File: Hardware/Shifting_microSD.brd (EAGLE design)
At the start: 18.3 x 25.1 mm, 20 parts, among them J1 USD_CONNECTOR, U1 TXB0104, U2 3.3V

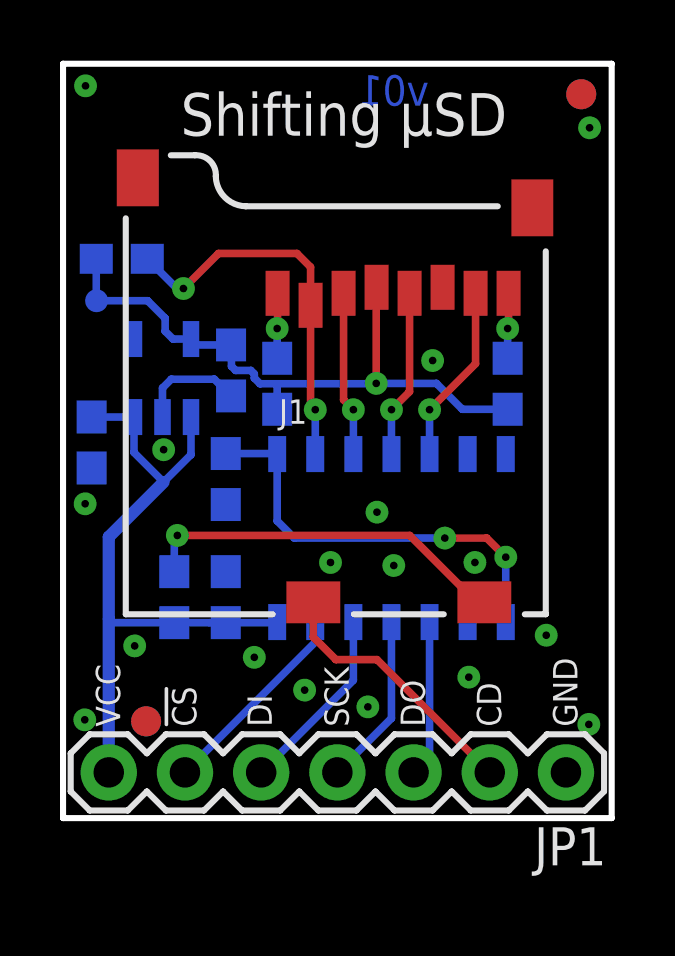
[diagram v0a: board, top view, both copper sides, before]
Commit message: Connected both 3.3V nets
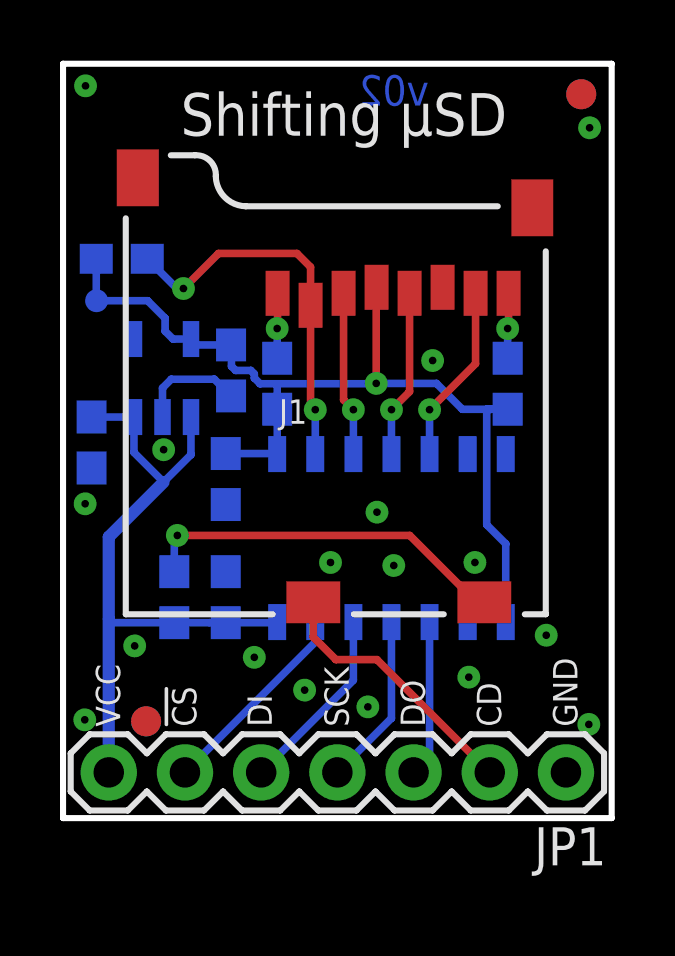
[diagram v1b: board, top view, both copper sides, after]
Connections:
- removed net 3.3V: C4.1, U1.1, U1.8
- net 3V3: now also C4.1, U1.1, U1.8
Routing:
- net 3.3V: track 14.2 -> 0.00 mm, vias 2 -> 0
- net 3V3: track 21.4 -> 32.7 mm
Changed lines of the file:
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@@
 <layers>
 <layer number="1" name="Top" color="4" fill="1" visible="yes" active="yes"/>
-<layer number="2" name="Route2" color="1" fill="3" visible="yes" active="yes"/>
-<layer number="3" name="Route3" color="4" fill="3" visible="yes" active="yes"/>
-<layer number="4" name="Route4" color="1" fill="4" visible="yes" active="yes"/>
-<layer number="5" name="Route5" color="4" fill="4" visible="yes" active="yes"/>
-<layer number="6" name="Route6" color="1" fill="8" visible="yes" active="yes"/>
-<layer number="7" name="Route7" color="4" fill="8" visible="yes" active="yes"/>
-<layer number="8" name="Route8" color="1" fill="2" visible="yes" active="yes"/>
-<layer number="9" name="Route9" color="4" fill="2" visible="yes" active="yes"/>
-<layer number="10" name="Route10" color="1" fill="7" visible="yes" active="yes"/>
-<layer number="11" name="Route11" color="4" fill="7" visible="yes" active="yes"/>
-<layer number="12" name="Route12" color="1" fill="5" visible="yes" active="yes"/>
-<layer number="13" name="Route13" color="4" fill="5" visible="yes" active="yes"/>
-<layer number="14" name="Route14" color="1" fill="6" visible="yes" active="yes"/>
-<layer number="15" name="Route15" color="4" fill="6" visible="yes" active="yes"/>
 <layer number="16" name="Bottom" color="1" fill="1" visible="yes" active="yes"/>
 <layer number="17" name="Pads" color="2" fill="1" visible="yes" active="yes"/>
@@
 </plain>
 <attributes>
-<attribute name="VERSION" value="v01"/>
+<attribute name="VERSION" value="v02"/>
 </attributes>
 <variantdefs>
@@
 <wire x1="1.1312" y1="17.2466" x2="1.1058" y2="17.272" width="0.254" layer="16"/>
 <wire x1="1.1312" y1="17.2466" x2="1.1176" y2="17.2466" width="0.254" layer="16"/>
+<contactref element="U1" pad="8"/>
+<contactref element="U1" pad="1"/>
+<wire x1="7.1374" y1="13.628" x2="7.1374" y2="12.1345" width="0.254" layer="16"/>
+<wire x1="14.8209" y1="13.628" x2="14.1224" y2="13.628" width="0.254" layer="16"/>
+<wire x1="14.1224" y1="13.628" x2="14.1224" y2="9.779" width="0.254" layer="16"/>
+<wire x1="14.1224" y1="9.779" x2="14.7574" y2="9.144" width="0.254" layer="16"/>
+<wire x1="14.7574" y1="9.144" x2="14.7574" y2="6.5345" width="0.254" layer="16"/>
+<contactref element="C4" pad="1"/>
+<wire x1="5.4229" y1="12.153" x2="7.1189" y2="12.153" width="0.254" layer="16"/>
+<wire x1="7.1189" y1="12.153" x2="7.1374" y2="12.1345" width="0.254" layer="16"/>
 </signal>
 <signal name="!CS_3V3">
@@
 <wire x1="3.7084" y1="6.516" x2="4.8768" y2="6.516" width="0.254" layer="16"/>
 </signal>
-<signal name="3.3V">
-<contactref element="U1" pad="1"/>
-<contactref element="C4" pad="1"/>
-<contactref element="U1" pad="8"/>
-<wire x1="5.4229" y1="12.153" x2="7.1189" y2="12.153" width="0.254" layer="16"/>
-<wire x1="7.1189" y1="12.153" x2="7.1374" y2="12.1345" width="0.254" layer="16"/>
-<wire x1="7.1374" y1="12.1345" x2="7.1374" y2="9.906" width="0.254" layer="16"/>
-<wire x1="7.1374" y1="9.906" x2="7.7089" y2="9.3345" width="0.254" layer="16"/>
-<wire x1="7.7089" y1="9.3345" x2="12.7254" y2="9.3345" width="0.254" layer="16"/>
-<wire x1="14.7574" y1="8.6995" x2="14.7574" y2="6.5345" width="0.254" layer="16"/>
-<via x="12.7254" y="9.3345" extent="1-16" drill="0.254"/>
-<wire x1="12.7254" y1="9.3345" x2="14.1224" y2="9.3345" width="0.254" layer="1"/>
-<wire x1="14.1224" y1="9.3345" x2="14.7574" y2="8.6995" width="0.254" layer="1"/>
-<via x="14.7574" y="8.6995" extent="1-16" drill="0.254"/>
-</signal>
 <signal name="SCK_3V3">

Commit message: Incremented to v10
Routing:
- net GND: vias 17 -> 18
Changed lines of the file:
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@@
 <setting verticaltext="up"/>
 </settings>
-<grid distance="0.001" unitdist="inch" unit="inch" style="lines" multiple="1" display="yes" altdistance="0.001" altunitdist="inch" altunit="inch"/>
+<grid distance="0.001" unitdist="inch" unit="mil" style="lines" multiple="1" display="yes" altdistance="0.001" altunitdist="inch" altunit="inch"/>
 <layers>
 <layer number="1" name="Top" color="4" fill="1" visible="yes" active="yes"/>
@@
 </plain>
 <attributes>
-<attribute name="VERSION" value="v02"/>
+<attribute name="VERSION" value="v10"/>
 </attributes>
 <variantdefs>
@@
 <via x="3.3528" y="12.2809" extent="1-16" drill="0.254"/>
 <via x="12.319" y="15.2527" extent="1-16" drill="0.254"/>
+<via x="14.9098" y="10.1473" extent="1-16" drill="0.254"/>
 </signal>
 <signal name="VDD_IO">

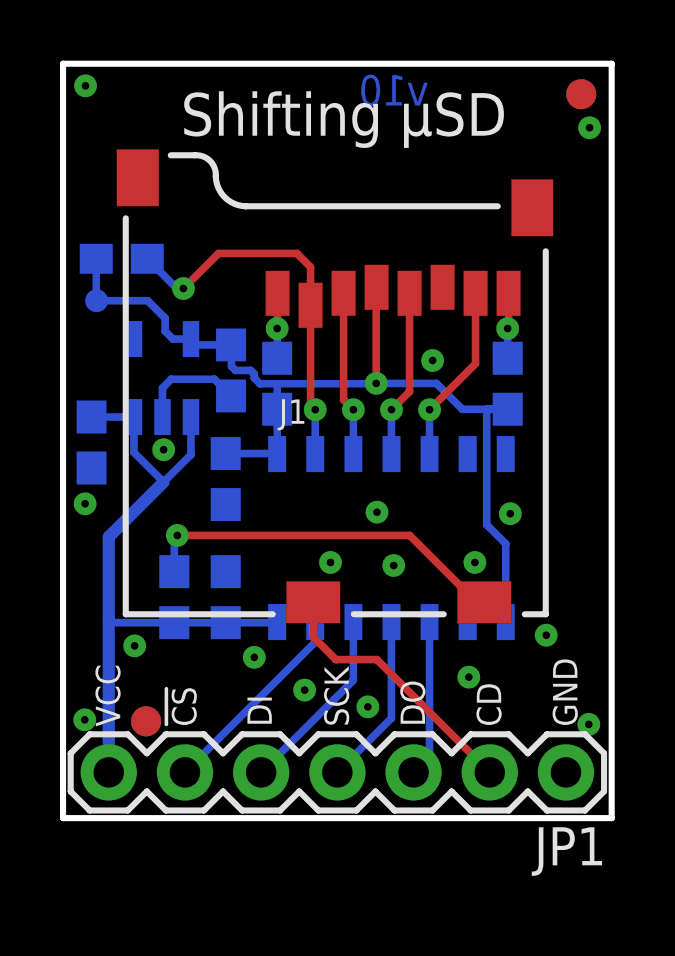
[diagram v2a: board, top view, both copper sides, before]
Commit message: Increased via sizes and shrunk PCB to exact width of header
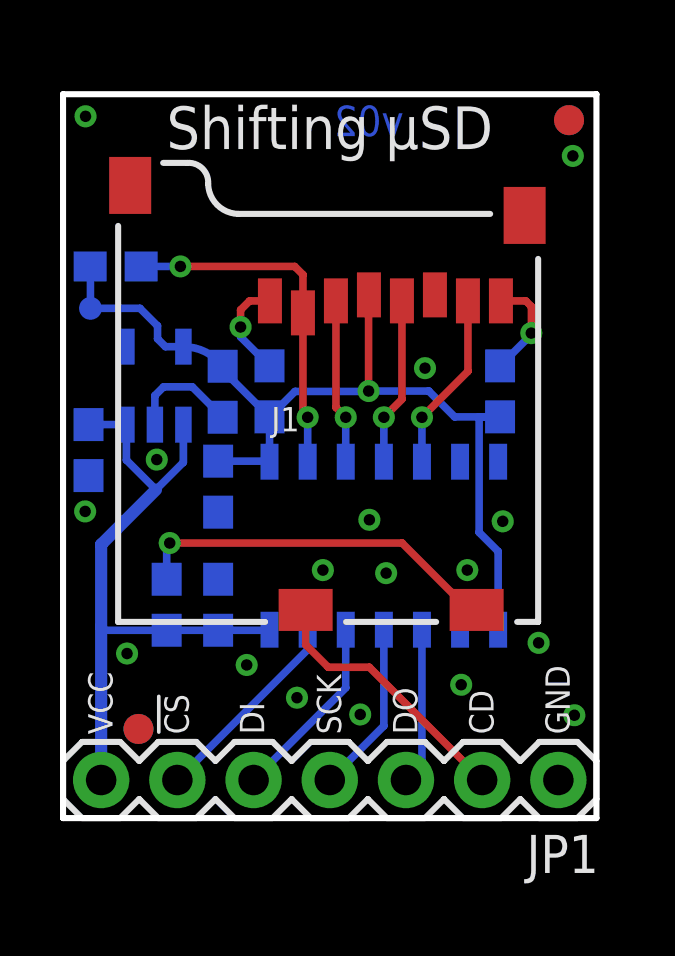
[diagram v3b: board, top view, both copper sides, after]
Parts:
- LOGO1: value SFE_LOGO_FLAME.3_INCH -> SFE_LOGO_FLAME.2_INCH; device SparkFun-Aesthetics:SFE_LOGO_FLAME_.3 -> SparkFun-Aesthetics:SFE_LOGO_FLAME_.2
- moved LOGO1 2.50 mm to (10.1, 17.6)
- moved FID1 0.95 mm to (16.9, 23.3)
- moved FID3 0.95 mm to (16.9, 23.3)
- moved C2 0.76 mm to (5.32, 14.2)
- moved C4 0.36 mm to (5.17, 11.0)
- moved J1 0.36 mm to (15.8, 6.54)
- moved C3 0.36 mm to (5.17, 7.11)
- moved R1 0.36 mm to (6.88, 14.2)
- moved FID2 0.36 mm to (2.51, 2.97)
- moved FID4 0.36 mm to (2.51, 2.97)
- moved R3 0.36 mm to (3.45, 7.11)
- moved U2 0.36 mm to (3.06, 14.4)
- moved R2 0.36 mm to (14.6, 14.2)
- moved U1 0.36 mm to (10.7, 9.08)
- moved JP1 0.36 mm to (16.5, 1.27)
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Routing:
- net RSV@2: track 2.18 -> 3.50 mm
- net RSV@1: track 2.18 -> 3.37 mm
- net !CS_3V3: track 12.9 -> 11.9 mm
- net 3V3: track 32.7 -> 32.0 mm
- net GND: track 3.61 -> 3.77 mm, vias 18 -> 17
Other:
- board size 18.3 x 25.1 mm -> 17.8 x 24.1 mm

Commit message: warped a trace
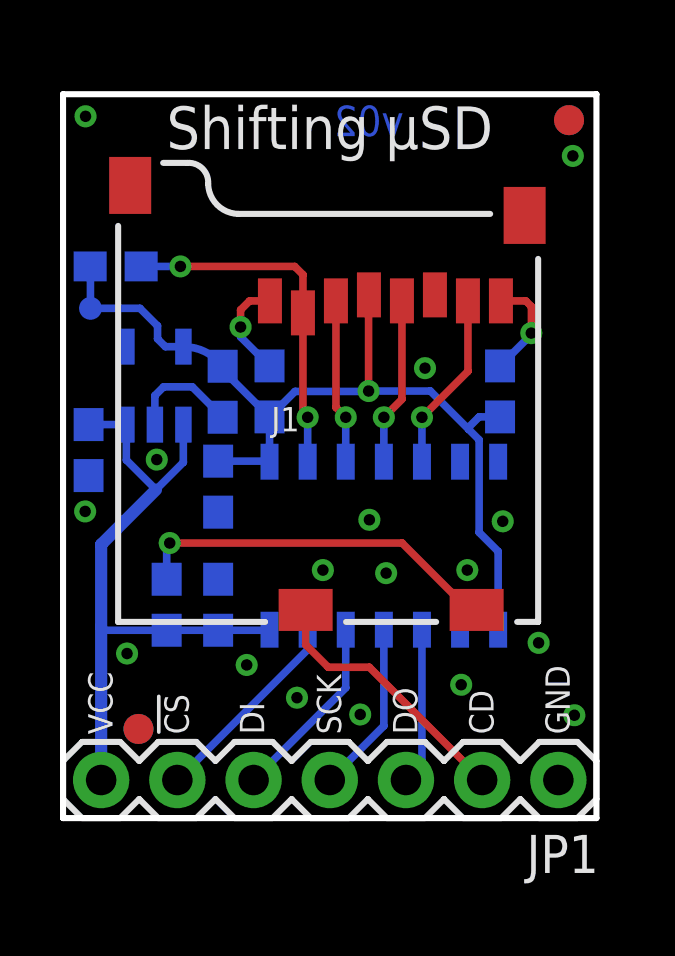
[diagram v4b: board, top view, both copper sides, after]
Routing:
- net 3V3: track 32.0 -> 31.4 mm
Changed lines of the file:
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@@
 <contactref element="U2" pad="5"/>
 <contactref element="C2" pad="1"/>
-<wire x1="14.5669" y1="13.374" x2="13.0547" y2="13.374" width="0.254" layer="16"/>
-<wire x1="12.192" y1="14.2367" x2="10.1854" y2="14.2367" width="0.254" layer="16"/>
+<wire x1="12.2428" y1="14.2367" x2="10.1854" y2="14.2367" width="0.254" layer="16"/>
 <via x="10.1854" y="14.2367" extent="1-16" drill="0.381"/>
 <wire x1="10.1854" y1="14.2367" x2="10.1854" y2="17.429" width="0.254" layer="1"/>
 <wire x1="10.1854" y1="17.429" x2="10.1969" y2="17.4405" width="0.254" layer="1"/>
 <wire x1="10.1727" y1="14.224" x2="10.1854" y2="14.2367" width="0.254" layer="16"/>
-<wire x1="12.192" y1="14.2367" x2="13.0547" y2="13.374" width="0.254" layer="16"/>
+<wire x1="12.2428" y1="14.2367" x2="13.51915" y2="12.96035" width="0.254" layer="16"/>
 <contactref element="R4" pad="2"/>
+<wire x1="13.51915" y1="12.96035" x2="13.8684" y2="12.6111" width="0.254" layer="16"/>
 <wire x1="4.0107" y1="15.7146" x2="3.4116" y2="15.7146" width="0.254" layer="16"/>
 <wire x1="3.4116" y1="15.7146" x2="3.1496" y2="15.9766" width="0.254" layer="16"/>
@@
 <wire x1="6.8834" y1="13.374" x2="6.8834" y2="11.8805" width="0.254" layer="16"/>
 <wire x1="14.5669" y1="13.374" x2="13.8684" y2="13.374" width="0.254" layer="16"/>
-<wire x1="13.8684" y1="13.374" x2="13.8684" y2="9.525" width="0.254" layer="16"/>
 <wire x1="13.8684" y1="9.525" x2="14.5034" y2="8.89" width="0.254" layer="16"/>
 <wire x1="14.5034" y1="8.89" x2="14.5034" y2="6.2805" width="0.254" layer="16"/>
@@
 <wire x1="0.9144" y1="18.3896" x2="0.9144" y2="16.9926" width="0.254" layer="16"/>
 <wire x1="0.9144" y1="16.9926" x2="2.5654" y2="16.9926" width="0.254" layer="16"/>
+<wire x1="13.8684" y1="9.525" x2="13.8684" y2="12.6111" width="0.254" layer="16"/>
+<wire x1="13.8684" y1="13.374" x2="13.51915" y2="13.02475" width="0.254" layer="16"/>
+<wire x1="13.51915" y1="13.02475" x2="13.51915" y2="12.96035" width="0.254" layer="16"/>
 </signal>
 <signal name="!CS_3V3">

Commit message: Renamed a jack to JP and moved over a test point
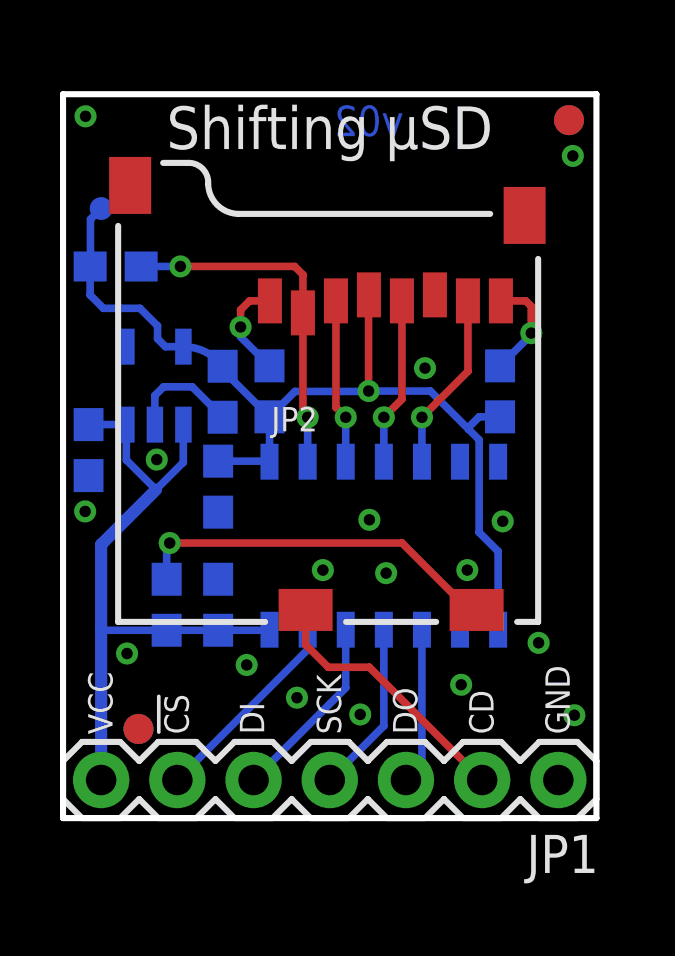
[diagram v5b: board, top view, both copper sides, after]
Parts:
- TP1: value TEST-POINT3 -> (none)
- moved TP1 3.35 mm to (1.27, 20.3)
- renumbered J1 to JP2
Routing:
- net 3V3: track 31.4 -> 33.2 mm
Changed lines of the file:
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@@
 <elements>
 <element name="FRAME1" library="SparkFun-Aesthetics" package="CREATIVE_COMMONS" value="FRAME-LETTER" x="-23.368" y="-9.779"/>
-<element name="J1" library="SparkFun-Connectors" package="MICRO-SD-SOCKET-PP" value="USD_CONNECTOR" x="15.8369" y="6.5405">
+<element name="JP2" library="SparkFun-Connectors" package="MICRO-SD-SOCKET-PP" value="USD_CONNECTOR" x="15.8369" y="6.5405">
 <attribute name="PROD_ID" value="CONN-07820" x="15.8369" y="6.5405" size="1.778" layer="27" display="off"/>
 </element>
@@
 <attribute name="PROD_ID" value="RES-07828" x="1.7526" y="18.3896" size="1.778" layer="28" rot="MR0" display="off"/>
 </element>
-<element name="TP1" library="SparkFun-Passives" package="PAD.03X.03" value="TEST-POINT3" x="0.9144" y="16.9926" rot="MR0"/>
+<element name="TP1" library="SparkFun-Passives" package="PAD.03X.03" value="" x="1.27" y="20.32" rot="MR0"/>
 </elements>
 <signals>
 <signal name="CD">
-<contactref element="J1" pad="CD2"/>
+<contactref element="JP2" pad="CD2"/>
 <contactref element="JP1" pad="2"/>
 <wire x1="8.0869" y1="6.9405" x2="8.0869" y2="5.7815" width="0.254" layer="1"/>
@@
 </signal>
 <signal name="3V3">
-<contactref element="J1" pad="VCC"/>
+<contactref element="JP2" pad="VCC"/>
 <contactref element="R1" pad="2"/>
 <contactref element="R2" pad="2"/>
@@
 <wire x1="4.0107" y1="15.7146" x2="5.3213" y2="15.0613" width="0.254" layer="16" curve="-52.990115"/>
 <wire x1="0.9026" y1="18.3896" x2="0.9144" y2="18.3896" width="0.254" layer="16"/>
-<wire x1="0.9144" y1="18.3896" x2="0.9144" y2="16.9926" width="0.254" layer="16"/>
-<wire x1="0.9144" y1="16.9926" x2="2.5654" y2="16.9926" width="0.254" layer="16"/>
 <wire x1="13.8684" y1="9.525" x2="13.8684" y2="12.6111" width="0.254" layer="16"/>
 <wire x1="13.8684" y1="13.374" x2="13.51915" y2="13.02475" width="0.254" layer="16"/>
 <wire x1="13.51915" y1="13.02475" x2="13.51915" y2="12.96035" width="0.254" layer="16"/>
+<wire x1="0.9144" y1="18.3896" x2="0.9144" y2="19.9644" width="0.254" layer="16"/>
+<wire x1="0.9144" y1="19.9644" x2="1.27" y2="20.32" width="0.254" layer="16"/>
+<wire x1="2.5654" y1="16.9926" x2="1.3462" y2="16.9926" width="0.254" layer="16"/>
+<wire x1="1.3462" y1="16.9926" x2="0.9026" y2="17.4362" width="0.254" layer="16"/>
+<wire x1="0.9026" y1="17.4362" x2="0.9026" y2="18.3896" width="0.254" layer="16"/>
 </signal>
 <signal name="!CS_3V3">
 <contactref element="U1" pad="2"/>
-<contactref element="J1" pad="CS"/>
+<contactref element="JP2" pad="CS"/>
 <wire x1="7.9969" y1="16.8405" x2="7.9969" y2="13.3604" width="0.254" layer="1"/>
 <wire x1="7.9969" y1="13.3604" x2="8.1534" y2="13.3604" width="0.254" layer="1"/>
@@
 <signal name="DI_3V3">
 <contactref element="U1" pad="3"/>
-<contactref element="J1" pad="DI"/>
+<contactref element="JP2" pad="DI"/>
 <wire x1="9.0969" y1="17.2405" x2="9.0969" y2="13.6869" width="0.254" layer="1"/>
 <via x="9.4234" y="13.3604" extent="1-16" drill="0.381"/>
@@
 </signal>
 <signal name="RSV@1">
-<contactref element="J1" pad="RSV1"/>
+<contactref element="JP2" pad="RSV1"/>
 <contactref element="R1" pad="1"/>
 <via x="5.9182" y="16.3703" extent="1-16" drill="0.381"/>
@@
 </signal>
 <signal name="RSV@2">
-<contactref element="J1" pad="RSV2"/>
+<contactref element="JP2" pad="RSV2"/>
 <contactref element="R2" pad="1"/>
 <via x="15.6083" y="16.1671" extent="1-16" drill="0.381"/>
@@
 </signal>
 <signal name="CDSDSD">
-<contactref element="J1" pad="CD1"/>
+<contactref element="JP2" pad="CD1"/>
 <contactref element="R3" pad="1"/>
 <wire x1="3.4544" y1="7.962" x2="3.4544" y2="9.0678" width="0.254" layer="16"/>
@@
 </polygon>
 <contactref element="JP1" pad="1"/>
-<contactref element="J1" pad="GND1"/>
-<contactref element="J1" pad="GND"/>
-<contactref element="J1" pad="GND3"/>
+<contactref element="JP2" pad="GND1"/>
+<contactref element="JP2" pad="GND"/>
+<contactref element="JP2" pad="GND3"/>
 <via x="17.0434" y="3.429" extent="1-16" drill="0.381"/>
 <via x="7.7978" y="4.0132" extent="1-16" drill="0.381"/>
@@
 </signal>
 <signal name="SCK_3V3">
-<contactref element="J1" pad="SCLK"/>
+<contactref element="JP2" pad="SCLK"/>
 <contactref element="U1" pad="4"/>
 <wire x1="11.2969" y1="17.2405" x2="11.2969" y2="13.9639" width="0.254" layer="1"/>
@@
 </signal>
 <signal name="DO_3V3">
-<contactref element="J1" pad="DO"/>
+<contactref element="JP2" pad="DO"/>
 <contactref element="U1" pad="5"/>
 <wire x1="13.4969" y1="17.2405" x2="13.4969" y2="14.8939" width="0.254" layer="1"/>

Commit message: updated version number for production
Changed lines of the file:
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@@
 </plain>
 <attributes>
-<attribute name="VERSION" value="v02"/>
+<attribute name="VERSION" value="v10"/>
 </attributes>
 <variantdefs>
